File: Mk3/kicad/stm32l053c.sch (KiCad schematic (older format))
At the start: 20 parts, among them J1 CONN_01X04, P1 SWD, U1 AP2112, U2 STM32L053C8_LQFP48, U3 ADS1015, U4 EDGE_SMA, U5 RFM92/95

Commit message: Solar charging
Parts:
- removed J1: CONN_01X04, Pin_Headers:Pin_Header_Straight_1x04_Pitch2.54mm, symbol CONN_01X04
- added D2: D_Schottky, symbol D_Schottky
- added J1: CONN_01X02, symbol CONN_01X02
- added R5: R_Shunt, symbol R_Shunt
- added SC1: Solar_Cells, symbol Solar_Cells
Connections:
- net labels added: SOLAR
- net labels removed: +BATT
- wire segments 75 -> 71
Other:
- moved on the sheet: BT1, C1, C2, C3, C4, C5, C6, R4, U1, U2

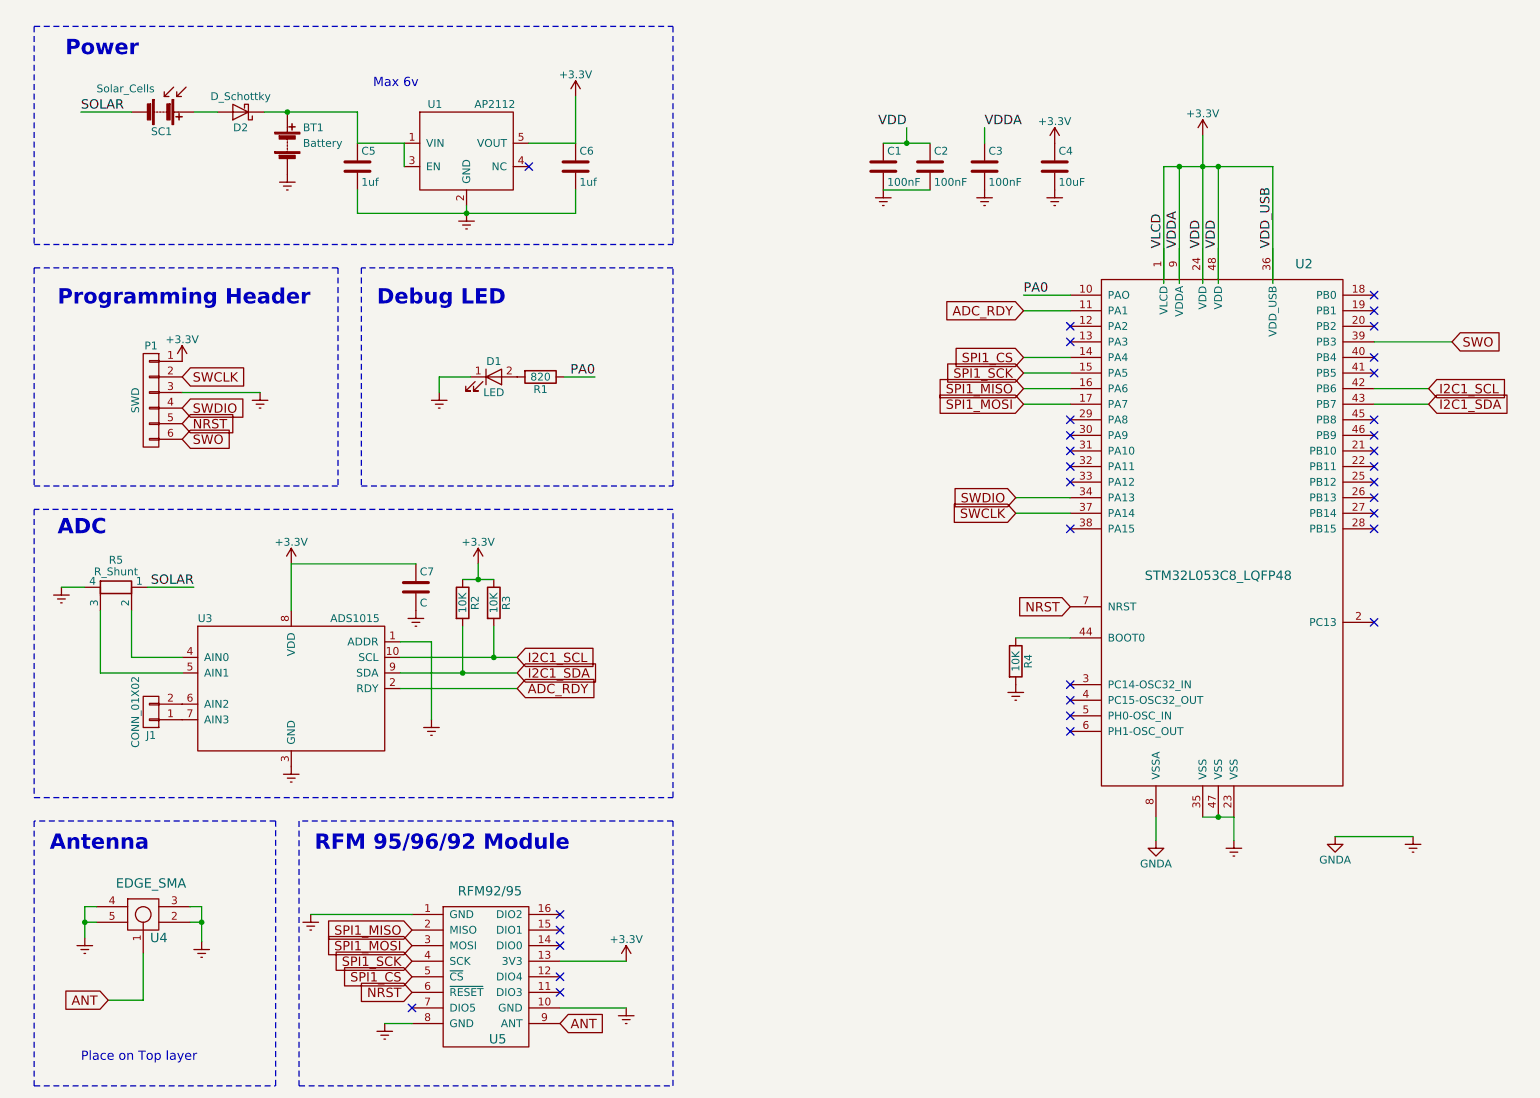
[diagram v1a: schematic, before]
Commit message: DIO1 from the RFM module
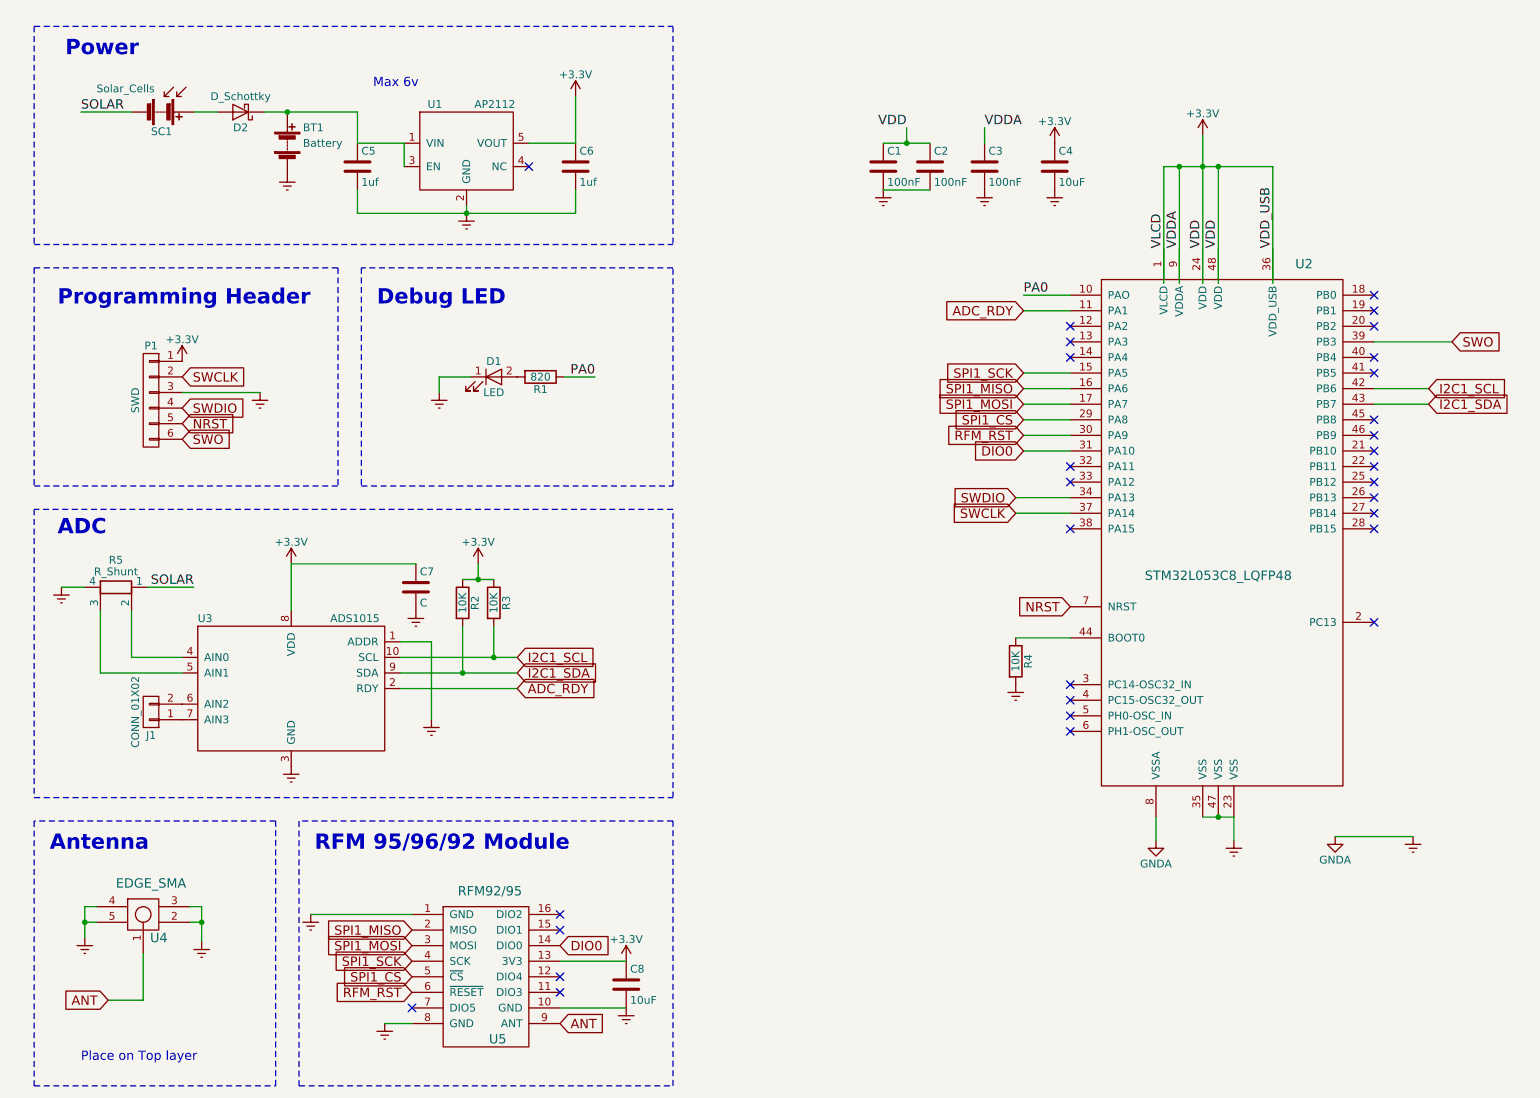
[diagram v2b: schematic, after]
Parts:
- added C8: 10uF, Capacitors_SMD:C_0805_HandSoldering, symbol C
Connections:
- net labels added: DIO0, RFM_RST
- wire segments 71 -> 73
- no-connect marks 33 -> 30
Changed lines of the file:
@@
 $EndDescr
 $Comp
-L Earth #PWR6
+L Earth #PWR5
 U 1 1 58021BE1
 P 6425 1775
-F 0 "#PWR6" H 6425 1525 50  0001 C CNN
+F 0 "#PWR5" H 6425 1525 50  0001 C CNN
 F 1 "Earth" H 6425 1625 50  0001 C CNN
 F 2 "" H 6425 1775 50  0000 C CNN
@@
 $EndComp
 $Comp
-L GNDA #PWR10
+L GNDA #PWR19
 U 1 1 58021F75
 P 9325 5925
-F 0 "#PWR10" H 9325 5675 50  0001 C CNN
+F 0 "#PWR19" H 9325 5675 50  0001 C CNN
 F 1 "GNDA" H 9325 5775 50  0000 C CNN
 F 2 "" H 9325 5925 50  0000 C CNN
@@
 $EndComp
 $Comp
-L Earth #PWR11
+L Earth #PWR20
 U 1 1 58021F89
 P 9825 5925
-F 0 "#PWR11" H 9825 5675 50  0001 C CNN
+F 0 "#PWR20" H 9825 5675 50  0001 C CNN
 F 1 "Earth" H 9825 5775 50  0001 C CNN
 F 2 "" H 9825 5925 50  0000 C CNN
@@
 $EndComp
 $Comp
-L GNDA #PWR24
+L GNDA #PWR21
 U 1 1 58022154
 P 8175 5950
-F 0 "#PWR24" H 8175 5700 50  0001 C CNN
+F 0 "#PWR21" H 8175 5700 50  0001 C CNN
 F 1 "GNDA" H 8175 5800 50  0000 C CNN
 F 2 "" H 8175 5950 50  0000 C CNN
@@
 $EndComp
 $Comp
-L Earth #PWR25
+L Earth #PWR22
 U 1 1 580221FA
 P 8675 5950
-F 0 "#PWR25" H 8675 5700 50  0001 C CNN
+F 0 "#PWR22" H 8675 5700 50  0001 C CNN
 F 1 "Earth" H 8675 5800 50  0001 C CNN
 F 2 "" H 8675 5950 50  0000 C CNN
@@
 $EndComp
 $Comp
-L Earth #PWR15
+L Earth #PWR10
 U 1 1 580369A9
 P 2425 3075
-F 0 "#PWR15" H 2425 2825 50  0001 C CNN
+F 0 "#PWR10" H 2425 2825 50  0001 C CNN
 F 1 "Earth" H 2425 2925 50  0001 C CNN
 F 2 "" H 2425 3075 50  0000 C CNN
@@
 PA0
 $Comp
-L Earth #PWR8
+L Earth #PWR7
 U 1 1 58039244
 P 7525 1775
-F 0 "#PWR8" H 7525 1525 50  0001 C CNN
+F 0 "#PWR7" H 7525 1525 50  0001 C CNN
 F 1 "Earth" H 7525 1625 50  0001 C CNN
 F 2 "" H 7525 1775 50  0000 C CNN
@@
 $EndComp
 $Comp
-L Earth #PWR7
+L Earth #PWR6
 U 1 1 5803BDC8
 P 7075 1775
-F 0 "#PWR7" H 7075 1525 50  0001 C CNN
+F 0 "#PWR6" H 7075 1525 50  0001 C CNN
 F 1 "Earth" H 7075 1625 50  0001 C CNN
 F 2 "" H 7075 1775 50  0000 C CNN
@@
 $EndComp
 $Comp
-L Earth #PWR21
+L Earth #PWR16
 U 1 1 58065816
 P 7275 4950
-F 0 "#PWR21" H 7275 4700 50  0001 C CNN
+F 0 "#PWR16" H 7275 4700 50  0001 C CNN
 F 1 "Earth" H 7275 4800 50  0001 C CNN
 F 2 "" H 7275 4950 50  0000 C CNN
@@
 $EndComp
 $Comp
-L Earth #PWR16
+L Earth #PWR11
 U 1 1 58077163
 P 3575 3075
-F 0 "#PWR16" H 3575 2825 50  0001 C CNN
+F 0 "#PWR11" H 3575 2825 50  0001 C CNN
 F 1 "Earth" H 3575 2925 50  0001 C CNN
 F 2 "" H 3575 3075 50  0000 C CNN
@@
 $EndComp
 $Comp
-L Earth #PWR23
+L Earth #PWR18
 U 1 1 592DF55A
 P 2625 5475
-F 0 "#PWR23" H 2625 5225 50  0001 C CNN
+F 0 "#PWR18" H 2625 5225 50  0001 C CNN
 F 1 "Earth" H 2625 5325 50  0001 C CNN
 F 2 "" H 2625 5475 50  0000 C CNN
@@
 NoConn ~ 4150 1625
 $Comp
-L Earth #PWR12
+L Earth #PWR8
 U 1 1 592F1C89
 P 3750 1925
-F 0 "#PWR12" H 3750 1675 50  0001 C CNN
+F 0 "#PWR8" H 3750 1675 50  0001 C CNN
 F 1 "Earth" H 3750 1775 50  0001 C CNN
 F 2 "" H 3750 1925 50  0000 C CNN
@@
 Text GLabel 3400 6625 0    60   Input ~ 0
 SPI1_MOSI
-Text GLabel 7325 2850 0    60   Input ~ 0
+Text GLabel 7325 3250 0    60   Input ~ 0
 SPI1_CS
 Text GLabel 3400 6825 0    60   Input ~ 0
 SPI1_CS
 Text GLabel 3400 6925 0    60   Input ~ 0
-NRST
-$Comp
-L +3.3V #PWR2
+RFM_RST
+$Comp
+L +3.3V #PWR1
 U 1 1 592F43A5
 P 4450 1175
-F 0 "#PWR2" H 4450 1025 50  0001 C CNN
+F 0 "#PWR1" H 4450 1025 50  0001 C CNN
 F 1 "+3.3V" H 4450 1315 50  0000 C CNN
 F 2 "" H 4450 1175 50  0001 C CNN
@@
 $EndComp
 $Comp
-L +3.3V #PWR14
+L +3.3V #PWR9
 U 1 1 592F4BC3
 P 1925 2875
-F 0 "#PWR14" H 1925 2725 50  0001 C CNN
+F 0 "#PWR9" H 1925 2725 50  0001 C CNN
 F 1 "+3.3V" H 1925 3015 50  0000 C CNN
 F 2 "" H 1925 2875 50  0001 C CNN
@@
 $EndComp
 $Comp
-L +3.3V #PWR5
+L +3.3V #PWR2
 U 1 1 592F4E66
 P 8475 1425
-F 0 "#PWR5" H 8475 1275 50  0001 C CNN
+F 0 "#PWR2" H 8475 1275 50  0001 C CNN
 F 1 "+3.3V" H 8475 1565 50  0000 C CNN
 F 2 "" H 8475 1425 50  0001 C CNN
@@
 $EndComp
 $Comp
-L +3.3V #PWR29
+L +3.3V #PWR26
 U 1 1 592F53D7
 P 4775 6725
-F 0 "#PWR29" H 4775 6575 50  0001 C CNN
+F 0 "#PWR26" H 4775 6575 50  0001 C CNN
 F 1 "+3.3V" H 4775 6865 50  0000 C CNN
 F 2 "" H 4775 6725 50  0001 C CNN
@@
 $EndComp
 $Comp
-L +3.3V #PWR4
+L +3.3V #PWR3
 U 1 1 592F54CD
 P 7525 1475
-F 0 "#PWR4" H 7525 1325 50  0001 C CNN
+F 0 "#PWR3" H 7525 1325 50  0001 C CNN
 F 1 "+3.3V" H 7525 1615 50  0000 C CNN
 F 2 "" H 7525 1475 50  0001 C CNN
@@
 NoConn ~ 7625 2650
 NoConn ~ 7625 2750
-NoConn ~ 7625 3250
-NoConn ~ 7625 3350
-NoConn ~ 7625 3450
+NoConn ~ 9575 2450
+NoConn ~ 7625 2850
 NoConn ~ 7625 3550
 NoConn ~ 7625 3650
 NoConn ~ 7625 3950
-NoConn ~ 9575 2450
 NoConn ~ 9575 2550
 NoConn ~ 9575 2850
@@
 NoConn ~ 4350 6425
 NoConn ~ 4350 6525
-NoConn ~ 4350 6625
 NoConn ~ 4350 6825
 NoConn ~ 4350 6925
 NoConn ~ 3400 7025
 $Comp
-L Earth #PWR30
+L Earth #PWR27
 U 1 1 592F7C8A
 P 4775 7025
-F 0 "#PWR30" H 4775 6775 50  0001 C CNN
+F 0 "#PWR27" H 4775 6775 50  0001 C CNN
 F 1 "Earth" H 4775 6875 50  0001 C CNN
 F 2 "" H 4775 7025 50  0000 C CNN
@@
 $EndComp
 $Comp
-L Earth #PWR26
+L Earth #PWR23
 U 1 1 592F7CF0
 P 2750 6425
-F 0 "#PWR26" H 2750 6175 50  0001 C CNN
+F 0 "#PWR23" H 2750 6175 50  0001 C CNN
 F 1 "Earth" H 2750 6275 50  0001 C CNN
 F 2 "" H 2750 6425 50  0000 C CNN
@@
 $EndComp
 $Comp
-L Earth #PWR31
+L Earth #PWR28
 U 1 1 592F7EE4
 P 3225 7125
-F 0 "#PWR31" H 3225 6875 50  0001 C CNN
+F 0 "#PWR28" H 3225 6875 50  0001 C CNN
 F 1 "Earth" H 3225 6975 50  0001 C CNN
 F 2 "" H 3225 7125 50  0000 C CNN
@@
 $EndComp
 $Comp
-L Earth #PWR27
+L Earth #PWR24
 U 1 1 592F80DC
 P 1300 6575
-F 0 "#PWR27" H 1300 6325 50  0001 C CNN
+F 0 "#PWR24" H 1300 6325 50  0001 C CNN
 F 1 "Earth" H 1300 6425 50  0001 C CNN
 F 2 "" H 1300 6575 50  0000 C CNN
@@
 $EndComp
 $Comp
-L Earth #PWR28
+L Earth #PWR25
 U 1 1 592F814F
 P 2050 6600
-F 0 "#PWR28" H 2050 6350 50  0001 C CNN
+F 0 "#PWR25" H 2050 6350 50  0001 C CNN
 F 1 "Earth" H 2050 6450 50  0001 C CNN
 F 2 "" H 2050 6600 50  0000 C CNN
@@
 $EndComp
 $Comp
-L Earth #PWR22
+L Earth #PWR17
 U 1 1 59301904
 P 3525 5175
-F 0 "#PWR22" H 3525 4925 50  0001 C CNN
+F 0 "#PWR17" H 3525 4925 50  0001 C CNN
 F 1 "Earth" H 3525 5025 50  0001 C CNN
 F 2 "" H 3525 5175 50  0000 C CNN
@@
 $EndComp
 $Comp
-L Earth #PWR20
+L Earth #PWR15
 U 1 1 593024E3
 P 3425 4475
-F 0 "#PWR20" H 3425 4225 50  0001 C CNN
+F 0 "#PWR15" H 3425 4225 50  0001 C CNN
 F 1 "Earth" H 3425 4325 50  0001 C CNN
 F 2 "" H 3425 4475 50  0000 C CNN
@@
 $EndComp
 $Comp
-L +3.3V #PWR17
+L +3.3V #PWR12
 U 1 1 59303669
 P 2625 4175
-F 0 "#PWR17" H 2625 4025 50  0001 C CNN
+F 0 "#PWR12" H 2625 4025 50  0001 C CNN
 F 1 "+3.3V" H 2625 4315 50  0000 C CNN
 F 2 "" H 2625 4175 50  0001 C CNN
@@
 $EndComp
 $Comp
-L +3.3V #PWR18
+L +3.3V #PWR13
 U 1 1 59303771
 P 3825 4175
-F 0 "#PWR18" H 3825 4025 50  0001 C CNN
+F 0 "#PWR13" H 3825 4025 50  0001 C CNN
 F 1 "+3.3V" H 3825 4315 50  0000 C CNN
 F 2 "" H 3825 4175 50  0001 C CNN
@@
 $EndComp
 $Comp
-L Earth #PWR9
+L Earth #PWR4
 U 1 1 59316863
 P 2600 1675
-F 0 "#PWR9" H 2600 1425 50  0001 C CNN
+F 0 "#PWR4" H 2600 1425 50  0001 C CNN
 F 1 "Earth" H 2600 1525 50  0001 C CNN
 F 2 "" H 2600 1675 50  0000 C CNN
@@
 $EndComp
 $Comp
-L Earth #PWR19
+L Earth #PWR14
 U 1 1 593290F6
 P 1150 4325
-F 0 "#PWR19" H 1150 4075 50  0001 C CNN
+F 0 "#PWR14" H 1150 4075 50  0001 C CNN
 F 1 "Earth" H 1150 4175 50  0001 C CNN
 F 2 "" H 1150 4325 50  0000 C CNN
@@
 Wire Wire Line
 	7625 2950 7325 2950
-Wire Wire Line
-	7325 2850 7625 2850
 Wire Wire Line
 	7325 2450 7625 2450
@@
 	6575 1375 6575 1475
 Connection ~ 6575 1475
+Text GLabel 7325 3350 0    60   Input ~ 0
+RFM_RST
+Text GLabel 4350 6625 2    60   Input ~ 0
+DIO0
+Text GLabel 7325 3450 0    60   Input ~ 0
+DIO0
+Wire Wire Line
+	7325 3250 7625 3250
+Wire Wire Line
+	7625 3350 7325 3350
+Wire Wire Line
+	7325 3450 7625 3450
+$Comp
+L C C8
+U 1 1 5933CA6B
+P 4775 6875
+F 0 "C8" H 4800 6975 50  0000 L CNN
+F 1 "10uF" H 4800 6775 50  0000 L CNN
+F 2 "Capacitors_SMD:C_0805_HandSoldering" H 4813 6725 50  0001 C CNN
+F 3 "" H 4775 6875 50  0000 C CNN
+	1    4775 6875
+	1    0    0    -1
+$EndComp
 $EndSCHEMATC
